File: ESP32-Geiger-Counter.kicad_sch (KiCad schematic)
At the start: 42 parts, among them J1 USB_C_Receptacle_USB2.0_16P, Q1 Q_NPN_BCE, Q2 Q_NPN_BCE, SW1 SW_Push, SW2 SW_Push, U1 TP4056-42-ESOP8, U2 USBLC6-2SC6, U3 ESP32-WROOM-32, U4 TPS63031DSK, U6 CP2102N-Axx-xQFN24

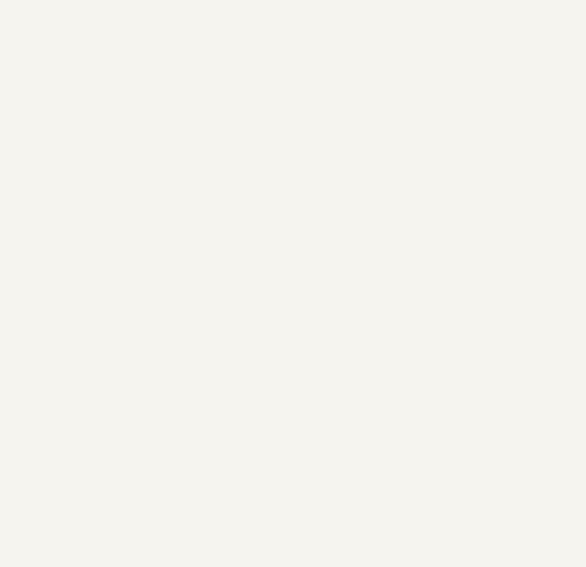
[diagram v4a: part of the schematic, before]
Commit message: added CUSTOM tube symbol
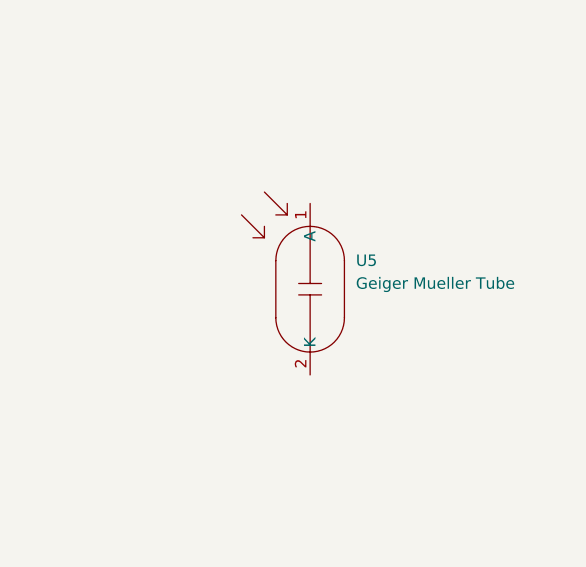
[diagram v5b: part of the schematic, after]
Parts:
- added U5: Geiger Mueller Tube, symbol Custom Parts:Geiger_Mueller_Tube
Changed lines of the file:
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@@
+	)
+	(symbol
+		(lib_id "Custom Parts:Geiger_Mueller_Tube")
+		(at 307.34 147.32 0)
+		(unit 1)
+		(body_style 1)
+		(exclude_from_sim no)
+		(in_bom yes)
+		(on_board yes)
+		(in_pos_files yes)
+		(dnp no)
+		(fields_autoplaced yes)
+		(property "Reference" "U5"
+			(at 316.23 147.3199 0)
+			(show_name no)
+			(do_not_autoplace no)
+			(effects
+				(font
+					(size 1.27 1.27)
+				)
+				(justify left)
+			)
+		)
+		(property "Value" "Geiger Mueller Tube"
+			(at 316.23 149.8599 0)
+			(show_name no)
+			(do_not_autoplace no)
+			(effects
+				(font
+					(size 1.27 1.27)
+				)
+				(justify left)
+			)
+		)
+		(property "Footprint" ""
+			(at 307.34 147.32 0)
+			(hide yes)
+			(show_name no)
+			(do_not_autoplace no)
+			(effects
+				(font
+					(size 1.27 1.27)
+				)
+			)
+		)
+		(property "Datasheet" ""
+			(at 307.34 147.32 0)
+			(hide yes)
+			(show_name no)
+			(do_not_autoplace no)
+			(effects
+				(font
+					(size 1.27 1.27)
+				)
+			)
+		)
+		(property "Description" ""
+			(at 307.34 147.32 0)
+			(hide yes)
+			(show_name no)
+			(do_not_autoplace no)
+			(effects
+				(font
+					(size 1.27 1.27)
+				)
+			)
+		)
+		(pin "1"
+		)
+		(pin "2"
+		)
+		(instances
+			(project "ESP32-Geiger-Counter"
+				(path "/1d04c1b6-b1c1-45fc-a2be-06365cafa415"
+					(reference "U5")
+					(unit 1)
+				)
+			)
+		)
 	)
 	(symbol

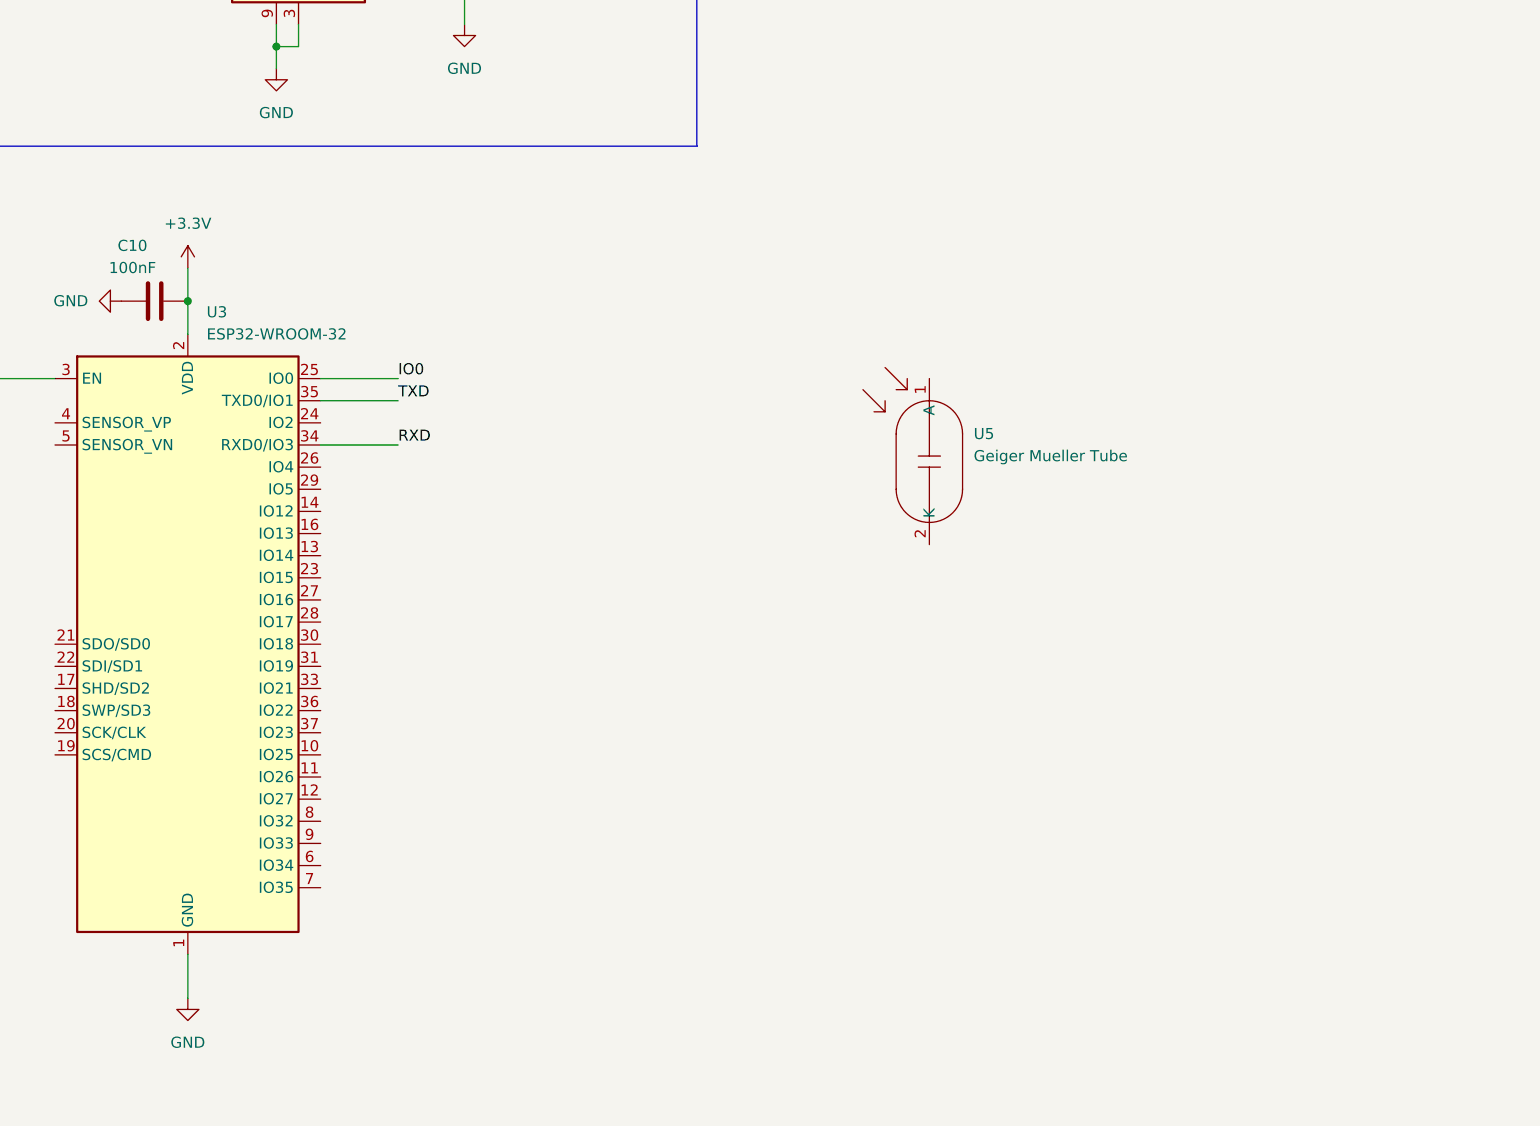
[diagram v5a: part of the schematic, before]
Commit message: swapped to use IC for 3.3v to 30v converter
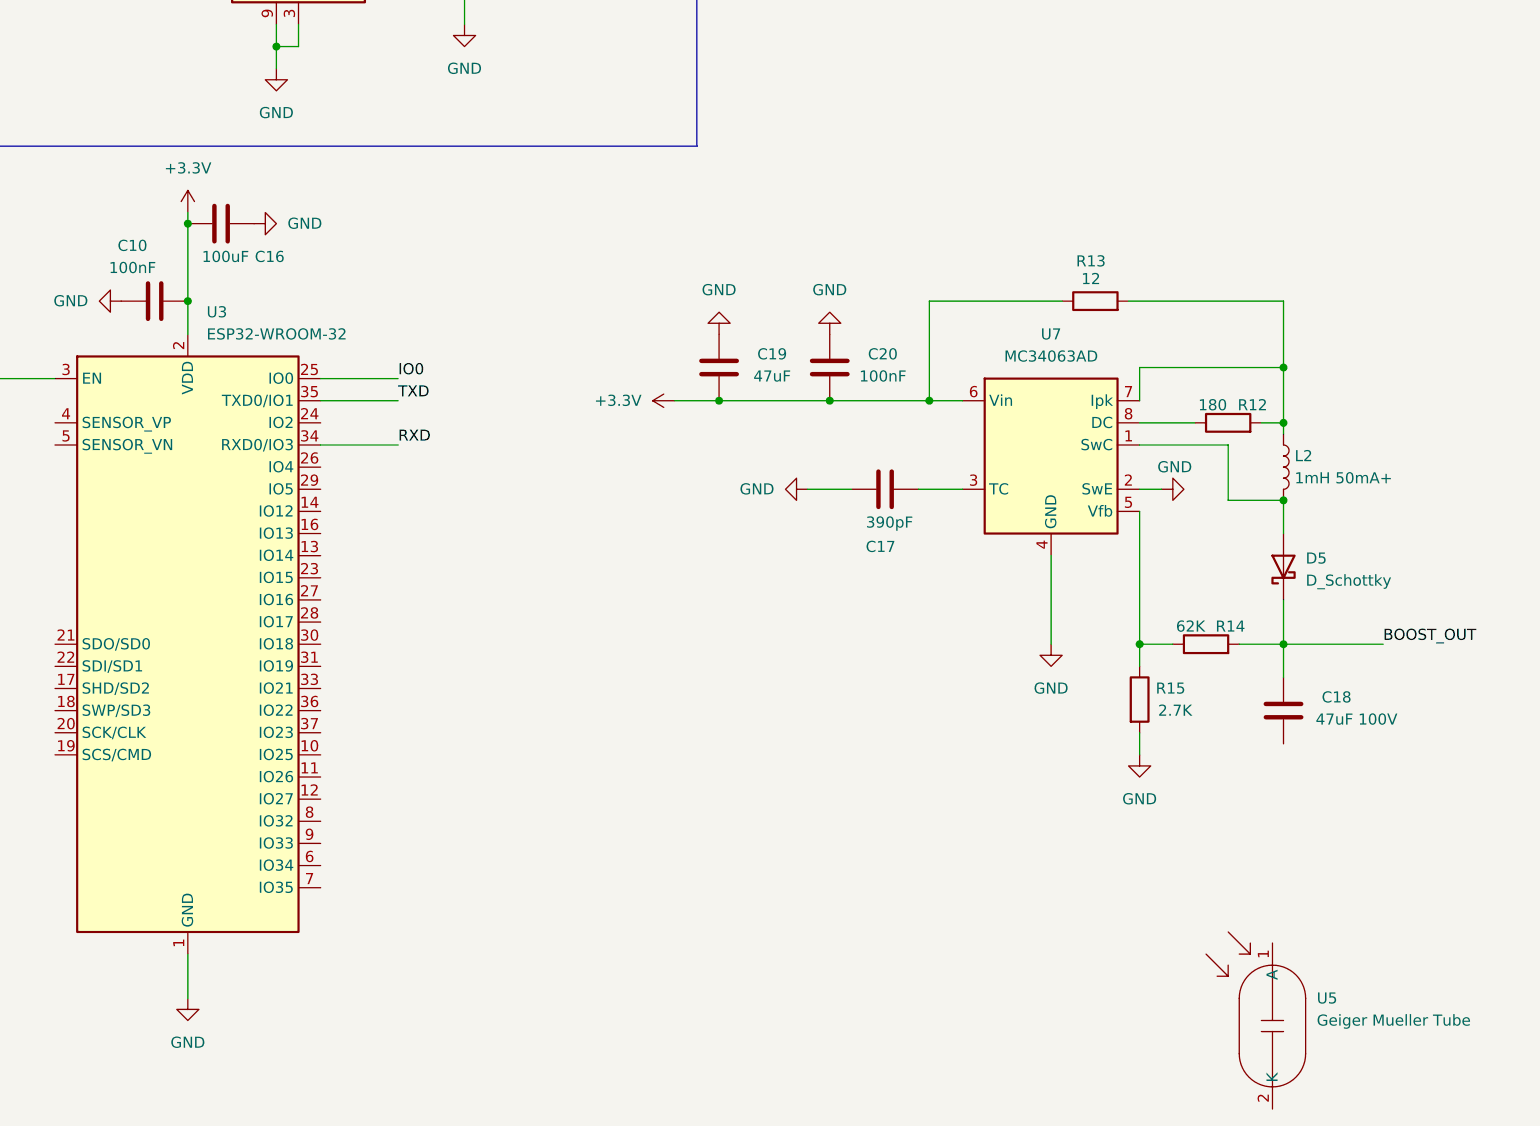
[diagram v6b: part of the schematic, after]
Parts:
- added C16: 100uF, symbol Device:C
- added C17: 390pF, symbol Device:C
- added C18: 47uF 100V, symbol Device:C
- added C19: 47uF, symbol Device:C
- added C20: 100nF, symbol Device:C
- added D5: D_Schottky, symbol Device:D_Schottky
- added L2: 1mH 50mA+, symbol Device:L
- added R12: 180, symbol Device:R
- added R13: 12, symbol Device:R
- added R14: 62K, symbol Device:R
- added R15: 2.7K, symbol Device:R
- added U7: MC34063AD, Package_SO:SOIC-8_3.9x4.9mm_P1.27mm, symbol Regulator_Switching:MC34063AD
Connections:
- net +3.3V: now also C16.2, C19.2, C20.2, R13.1, U7.6 (Vin)
- net GND: now also C16.1, C17.2, C19.1, C20.1, R15.2, U7.2 (SwE), U7.4 (GND)
- new net: R14.1, R15.1, U7.5 (Vfb)
- new net: D5.2 (A), L2.2, U7.1 (SwC)
- new net: C17.1, U7.3 (TC)
- new net: L2.1, R12.2, R13.2, U7.7 (Ipk)
- new net: R12.1, U7.8 (DC)
- new net BOOST_OUT: C18.1, D5.1 (K), R14.2
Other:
- moved on the sheet: U5

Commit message: idk if I will use this mega boost method
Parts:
- added C21, C22, C23, C24, C25, C26, C27, C28, C29, C30, C31, C32, C33, C34, C35, C36: 10nF 1kV, symbol Device:C
- added D10, D11, D12, D13, D14, D15, D16, D17, D18, D19, D20, D21, D6, D7, D8, D9: D, symbol Device:D
- L2: value 1mH 50mA+ -> 180uH
- R13: value 12 -> 2.2
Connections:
- net GND: now also C18.2, D5.2 (A), L2.2, U7.1 (SwC), C21.1, C22.1, D6.2 (A)
- net BOOST_OUT renamed VBOOST_30V
- new net: C21.2, C23.1, D6.1 (K), D7.2 (A)
- new net: C26.2, C28.1, D11.1 (K), D12.2 (A)
- new net: C25.2, C27.1, D10.1 (K), D11.2 (A)
- new net: C33.2, C35.1, D18.1 (K), D19.2 (A)
- new net: C32.2, C34.1, D17.1 (K), D18.2 (A)
- new net: C29.2, C31.1, D14.1 (K), D15.2 (A)
- new net: C28.2, C30.1, D13.1 (K), D14.2 (A)
- new net: C30.2, C32.1, D15.1 (K), D16.2 (A)
- new net: C35.2, D20.1 (K), D21.2 (A)
- new net: C34.2, C36.1, D19.1 (K), D20.2 (A)
- new net: C31.2, C33.1, D16.1 (K), D17.2 (A)
- new net: C22.2, C24.1, D7.1 (K), D8.2 (A)
- new net: C24.2, C26.1, D10.2 (A), D9.1 (K)
- new net: C23.2, C25.1, D8.1 (K), D9.2 (A)
- new net: C27.2, C29.1, D12.1 (K), D13.2 (A)
- new net 480V: C36.2, D21.1 (K)
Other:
- note added: "3.3V to ~30V"
- moved on the sheet: C10, C16, C17, C18, C19, C20, D5, L2, R12, R13, R14, R15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

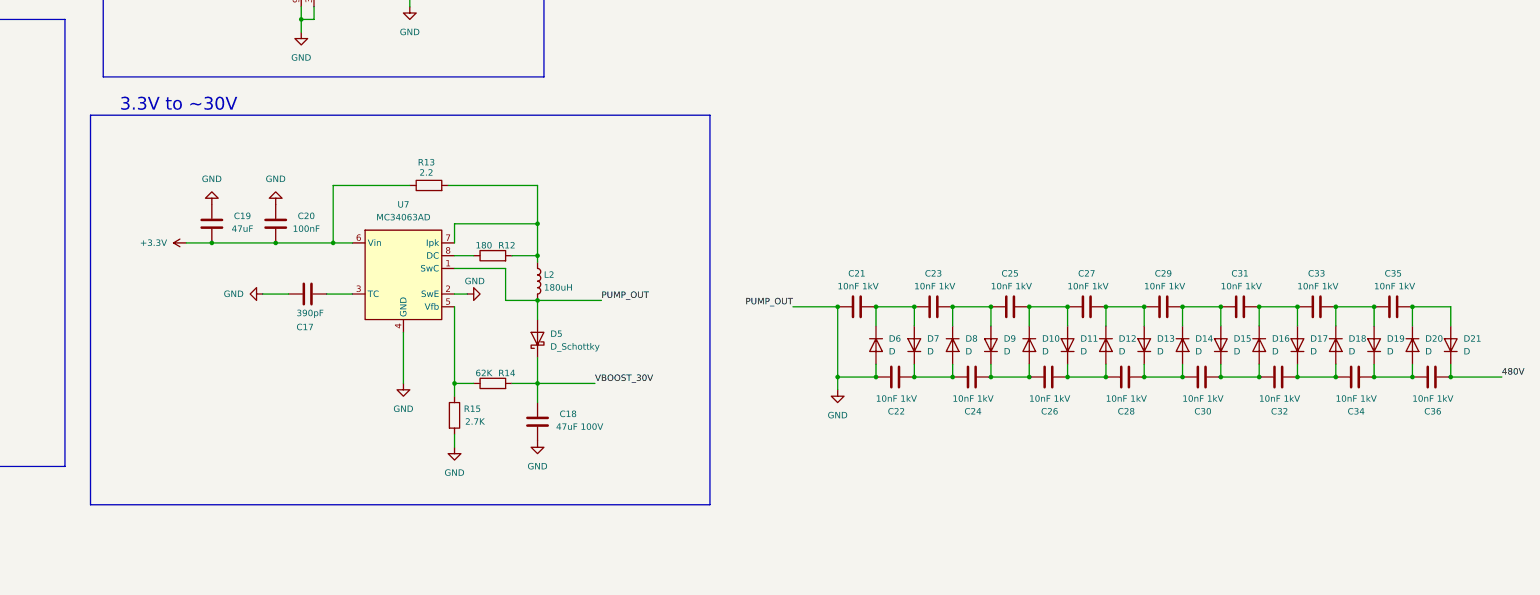
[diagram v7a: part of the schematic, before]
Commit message: removed the 3.3V to 30V
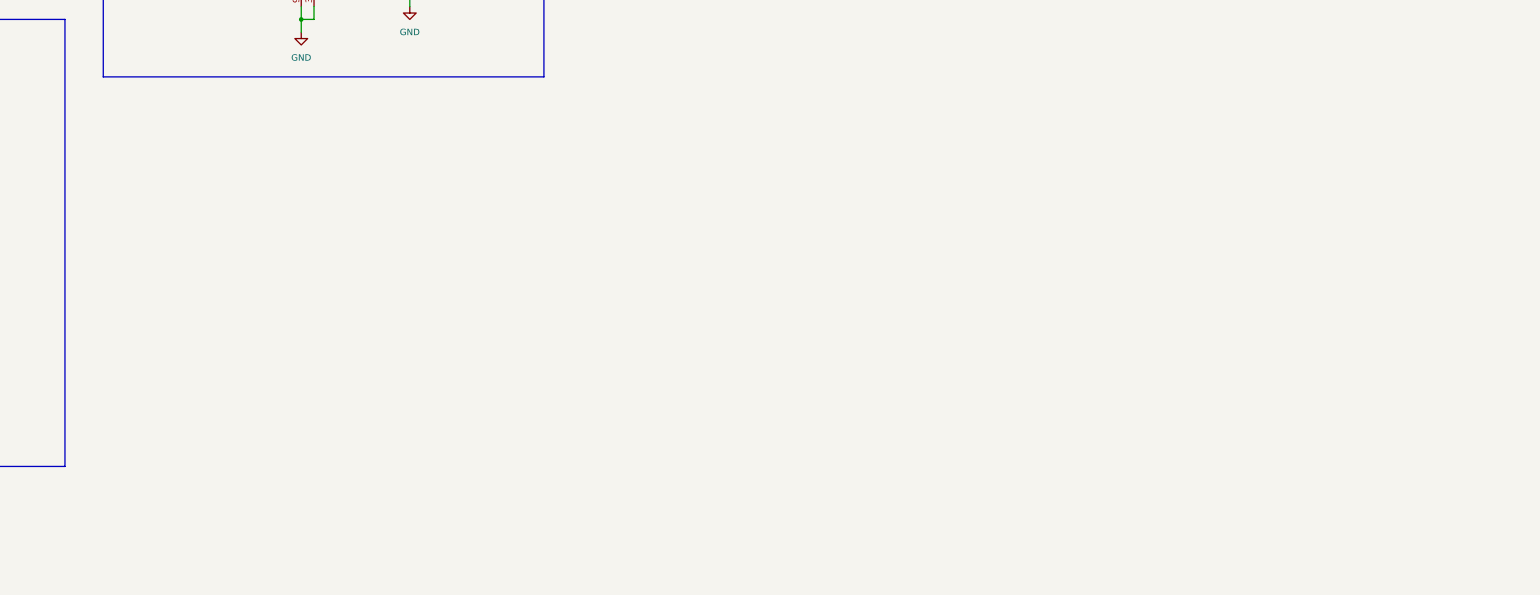
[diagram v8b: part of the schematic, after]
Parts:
- removed C17: 390pF, symbol Device:C
- removed C18: 47uF 100V, symbol Device:C
- removed C19: 47uF, symbol Device:C
- removed C20: 100nF, symbol Device:C
- removed C21, C22, C23, C24, C25, C26, C27, C28, C29, C30, C31, C32, C33, C34, C35, C36: 10nF 1kV, symbol Device:C
- removed D10, D11, D12, D13, D14, D15, D16, D17, D18, D19, D20, D21, D6, D7, D8, D9: D, symbol Device:D
- removed D5: D_Schottky, symbol Device:D_Schottky
- removed L2: 180uH, symbol Device:L
- removed R12: 180, symbol Device:R
- removed R13: 2.2, symbol Device:R
- removed R14: 62K, symbol Device:R
- removed R15: 2.7K, symbol Device:R
- removed U7: MC34063AD, Package_SO:SOIC-8_3.9x4.9mm_P1.27mm, symbol Regulator_Switching:MC34063AD
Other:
- note removed: "3.3V to ~30V"
